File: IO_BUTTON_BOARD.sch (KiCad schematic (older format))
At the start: 135 parts, among them P1 I2C, P10 IO_7, P2 I2C, P3 IO_0, P4 IO_1, P5 IO_2, P6 IO_3, P7 IO_4, P8 IO_5, P9 IO_6, Q1 NPN, Q10 PNP, Q11 PNP, Q12 PNP, Q13 PNP, Q14 PNP, Q15 PNP, Q16 PNP, Q17 PNP, Q2 PNP, Q3 NPN, Q4 PNP, Q5 NPN, Q6 NPN, Q7 PNP, Q8 PNP, Q9 NPN, SW1 CONFIG, SW10 SW_Push, SW11 SW_Push, SW12 SW_Push, SW13 SW_Push, SW14 SW_Push, SW15 SW_Push, SW16 SW_Push, SW17 SW_Push, SW2 SW_0, SW3 SW_1, SW4 SW_2, SW5 SW_3, SW6 SW_4, SW7 SW_5, SW8 SW_6, SW9 SW_7, U1 PCF8574A, U2 74HC86, U3 74HC86

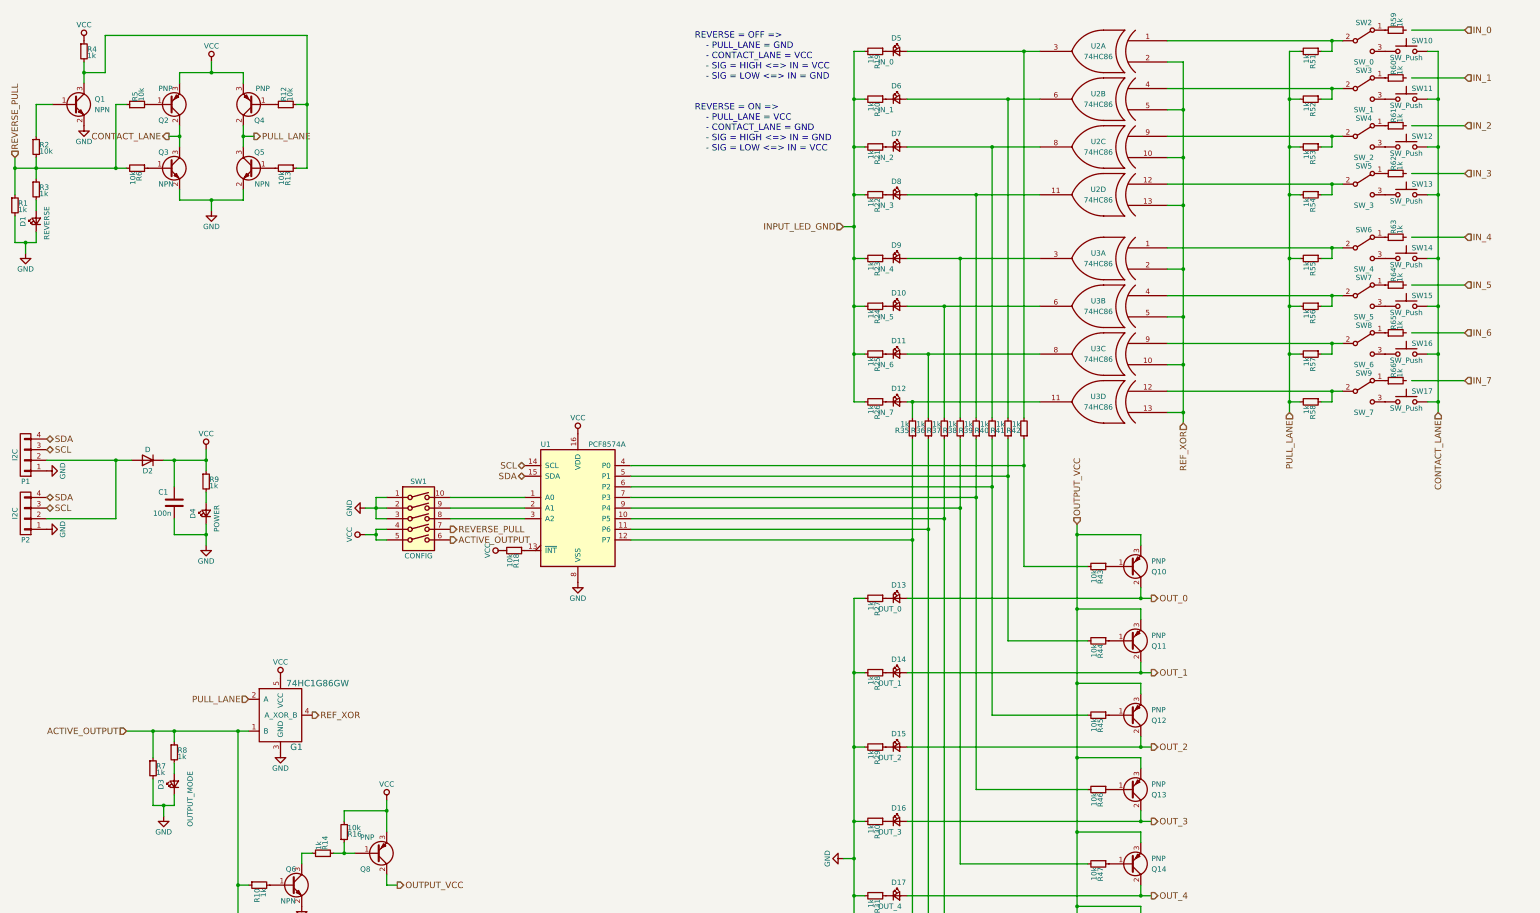
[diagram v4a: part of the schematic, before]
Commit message: Add manual routing, XOR gates remains to be routed
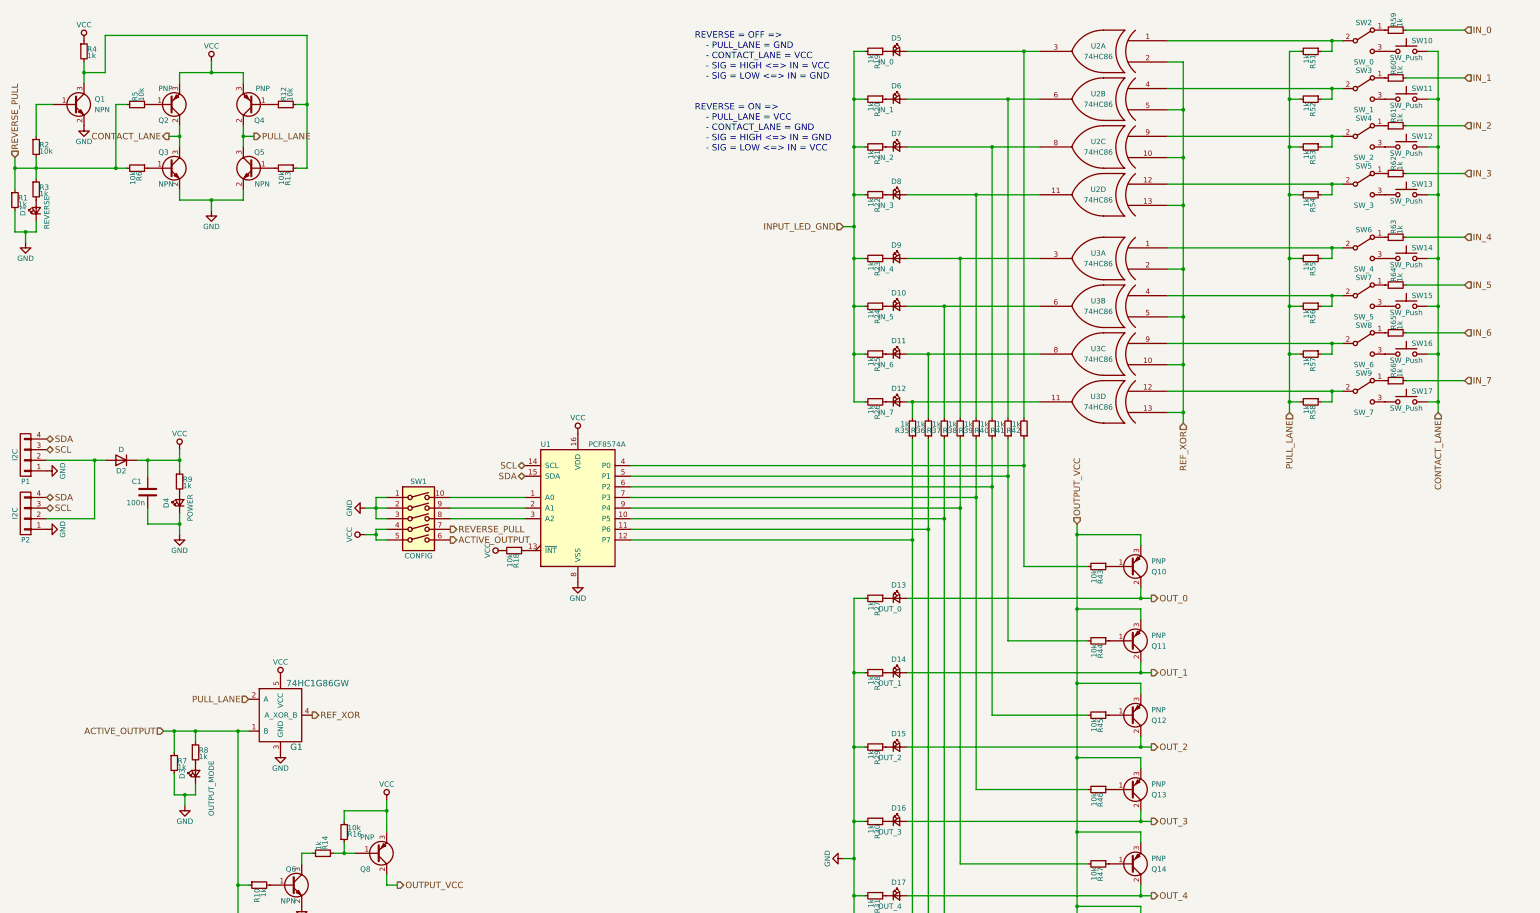
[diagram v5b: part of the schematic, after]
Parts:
- D2: footprint Diodes_SMD:DO-214AB_Handsoldering -> Diodes_SMD:DO-214AB
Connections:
- net IN_0: now also R59.2
- net IN_1: now also R60.2
- net IN_2: now also R61.2
- net IN_3: now also R62.2
- net IN_4: now also R63.2
- net IN_5: now also R64.2
- net IN_6: now also R65.2
- net IN_7: now also R66.2
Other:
- moved on the sheet: C1, D1, D2, D3, D4, R1, R7, R8, R9
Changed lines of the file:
@@
 Title "8_IO_BOARD"
 Date "2019-01-25"
-Rev "1.0"
+Rev "0.10"
 Comp "Mathias DELAHAYE"
 Comment1 "F4DEB"
@@
 L C C1
 U 1 1 5C4AF888
-P 2050 5050
-F 0 "C1" H 1900 5150 50  0000 L CNN
-F 1 "100n" H 1850 4950 50  0000 L CNN
-F 2 "Capacitors_SMD:c_elec_4x4.5" H 2088 4900 50  0001 C CNN
-F 3 "" H 2050 5050 50  0000 C CNN
-	1    2050 5050
+P 1800 4950
+F 0 "C1" H 1650 5050 50  0000 L CNN
+F 1 "100n" H 1600 4850 50  0000 L CNN
+F 2 "Capacitors_SMD:c_elec_4x4.5" H 1838 4800 50  0001 C CNN
+F 3 "" H 1800 4950 50  0000 C CNN
+	1    1800 4950
 	1    0    0    -1
 $EndComp
@@
 L LED_Small D4
 U 1 1 5C4B1934
-P 2350 5150
-F 0 "D4" H 2300 5275 50  0000 L CNN
-F 1 "POWER" H 2175 5050 50  0000 L CNN
-F 2 "LEDs:LED_0805" V 2350 5150 50  0001 C CNN
-F 3 "" V 2350 5150 50  0000 C CNN
-	1    2350 5150
+P 2100 5050
+F 0 "D4" H 2050 5175 50  0000 L CNN
+F 1 "POWER" H 1925 4950 50  0000 L CNN
+F 2 "LEDs:LED_0805" V 2100 5050 50  0001 C CNN
+F 3 "" V 2100 5050 50  0000 C CNN
+	1    2100 5050
 	0    -1   -1   0
 $EndComp
@@
 L R_Small R9
 U 1 1 5C4B193A
-P 2350 4850
-F 0 "R9" H 2380 4870 50  0000 L CNN
-F 1 "1k" H 2380 4810 50  0000 L CNN
-F 2 "Resistors_SMD:R_0805" H 2350 4850 50  0001 C CNN
-F 3 "" H 2350 4850 50  0000 C CNN
-	1    2350 4850
+P 2100 4850
+F 0 "R9" H 2130 4870 50  0000 L CNN
+F 1 "1k" H 2130 4810 50  0000 L CNN
+F 2 "Resistors_SMD:R_0805" H 2100 4850 50  0001 C CNN
+F 3 "" H 2100 4850 50  0000 C CNN
+	1    2100 4850
 	1    0    0    -1
 $EndComp
@@
 L R_Small R1
 U 1 1 5C4B8D83
-P 550 2250
-F 0 "R1" H 580 2270 50  0000 L CNN
-F 1 "1k" H 580 2210 50  0000 L CNN
-F 2 "Resistors_SMD:R_0805" H 550 2250 50  0001 C CNN
-F 3 "" H 550 2250 50  0000 C CNN
-	1    550  2250
+P 550 2200
+F 0 "R1" H 580 2220 50  0000 L CNN
+F 1 "1k" H 580 2160 50  0000 L CNN
+F 2 "Resistors_SMD:R_0805" H 550 2200 50  0001 C CNN
+F 3 "" H 550 2200 50  0000 C CNN
+	1    550  2200
 	1    0    0    -1
 $EndComp
@@
 L GND #PWR01
 U 1 1 5C4B8E84
-P 650 2700
-F 0 "#PWR01" H 650 2450 50  0001 C CNN
-F 1 "GND" H 650 2550 50  0000 C CNN
-F 2 "" H 650 2700 50  0000 C CNN
-F 3 "" H 650 2700 50  0000 C CNN
-	1    650  2700
+P 650 2600
+F 0 "#PWR01" H 650 2350 50  0001 C CNN
+F 1 "GND" H 650 2450 50  0000 C CNN
+F 2 "" H 650 2600 50  0000 C CNN
+F 3 "" H 650 2600 50  0000 C CNN
+	1    650  2600
 	1    0    0    -1
 $EndComp
@@
 L LED_Small D1
 U 1 1 5C4C4F1A
-P 750 2400
-F 0 "D1" H 700 2525 50  0000 L CNN
-F 1 "REVERSE" H 575 2300 50  0000 L CNN
-F 2 "LEDs:LED_0805" V 750 2400 50  0001 C CNN
-F 3 "" V 750 2400 50  0000 C CNN
-	1    750  2400
+P 750 2300
+F 0 "D1" H 700 2425 50  0000 L CNN
+F 1 "REVERSE" H 575 2200 50  0000 L CNN
+F 2 "LEDs:LED_0805" V 750 2300 50  0001 C CNN
+F 3 "" V 750 2300 50  0000 C CNN
+	1    750  2300
 	0    -1   -1   0
 $EndComp
@@
 L D D2
 U 1 1 5C6BAA14
-P 1800 4650
-F 0 "D2" H 1800 4750 50  0000 C CNN
-F 1 "D" H 1800 4550 50  0000 C CNN
-F 2 "Diodes_SMD:DO-214AB_Handsoldering" H 1800 4650 50  0001 C CNN
-F 3 "" H 1800 4650 50  0000 C CNN
-F 4 "688-0512" H 1800 4650 60  0001 C CNN "RS"
-	1    1800 4650
+P 1550 4650
+F 0 "D2" H 1550 4750 50  0000 C CNN
+F 1 "D" H 1550 4550 50  0000 C CNN
+F 2 "Diodes_SMD:DO-214AB" H 1550 4650 50  0001 C CNN
+F 3 "" H 1550 4650 50  0000 C CNN
+F 4 "688-0512" H 1550 4650 60  0001 C CNN "RS"
+	1    1550 4650
 	-1   0    0    1
 $EndComp
@@
 L VCC #PWR03
 U 1 1 5C767C53
-P 2350 4550
-F 0 "#PWR03" H 2350 4400 50  0001 C CNN
-F 1 "VCC" H 2350 4700 50  0000 C CNN
-F 2 "" H 2350 4550 50  0000 C CNN
-F 3 "" H 2350 4550 50  0000 C CNN
-	1    2350 4550
+P 2100 4550
+F 0 "#PWR03" H 2100 4400 50  0001 C CNN
+F 1 "VCC" H 2100 4700 50  0000 C CNN
+F 2 "" H 2100 4550 50  0000 C CNN
+F 3 "" H 2100 4550 50  0000 C CNN
+	1    2100 4550
 	1    0    0    -1
 $EndComp
@@
 L GND #PWR010
 U 1 1 5C7E9DBA
-P 2350 5450
-F 0 "#PWR010" H 2350 5200 50  0001 C CNN
-F 1 "GND" H 2350 5300 50  0000 C CNN
-F 2 "" H 2350 5450 50  0000 C CNN
-F 3 "" H 2350 5450 50  0000 C CNN
-	1    2350 5450
+P 2100 5350
+F 0 "#PWR010" H 2100 5100 50  0001 C CNN
+F 1 "GND" H 2100 5200 50  0000 C CNN
+F 2 "" H 2100 5350 50  0000 C CNN
+F 3 "" H 2100 5350 50  0000 C CNN
+	1    2100 5350
 	1    0    0    -1
 $EndComp
@@
 	0    1    1    0
 $EndComp
-Text HLabel 1600 7200 0    60   Input ~ 0
+Text HLabel 1950 7200 0    60   Input ~ 0
 ACTIVE_OUTPUT
 $Comp
@@
 Connection ~ 3950 5100
 Wire Wire Line
-	1500 5200 850  5200
-Wire Wire Line
-	850  4650 1650 4650
-Wire Wire Line
-	2350 5050 2350 4950
-Wire Wire Line
-	2350 4550 2350 4750
-Wire Wire Line
-	2350 5250 2350 5450
+	1300 5200 850  5200
+Wire Wire Line
+	850  4650 1400 4650
+Wire Wire Line
+	2100 4550 2100 4750
+Wire Wire Line
+	2100 5150 2100 5350
 Wire Wire Line
 	13850 800  13950 800
@@
 	3950 5300 4050 5300
 Wire Wire Line
-	550  1800 550  2150
+	550  1800 550  2100
 Wire Wire Line
 	2000 1600 2100 1600
@@
 	3300 650  3300 1900
 Wire Wire Line
-	750  2300 750  2200
-Wire Wire Line
-	550  2350 550  2600
-Wire Wire Line
-	550  2600 750  2600
-Wire Wire Line
-	750  2600 750  2500
-Wire Wire Line
-	650  2700 650  2600
-Connection ~ 650  2600
+	550  2300 550  2500
+Wire Wire Line
+	550  2500 750  2500
+Wire Wire Line
+	750  2500 750  2400
+Wire Wire Line
+	650  2600 650  2500
+Connection ~ 650  2500
 Wire Wire Line
 	1400 1000 1200 1000
@@
 Connection ~ 11150 6650
 Wire Wire Line
-	1500 4650 1500 5200
-Connection ~ 1500 4650
-Connection ~ 2050 4650
-Wire Wire Line
-	1950 4650 2350 4650
-Connection ~ 2350 4650
-Connection ~ 2350 5350
-Wire Wire Line
-	2050 4650 2050 4900
-Wire Wire Line
-	2050 5200 2050 5350
-Wire Wire Line
-	2050 5350 2350 5350
+	1300 4650 1300 5200
+Connection ~ 1300 4650
+Connection ~ 1800 4650
+Wire Wire Line
+	1700 4650 2100 4650
+Connection ~ 2100 4650
+Connection ~ 2100 5250
+Wire Wire Line
+	1800 4650 1800 4800
+Wire Wire Line
+	1800 5100 1800 5250
+Wire Wire Line
+	1800 5250 2100 5250
 Wire Wire Line
 	8950 5950 11250 5950
@@
 L R_Small R7
 U 1 1 5C821A26
-P 1850 7550
-F 0 "R7" H 1880 7570 50  0000 L CNN
-F 1 "1k" H 1880 7510 50  0000 L CNN
-F 2 "Resistors_SMD:R_0805" H 1850 7550 50  0001 C CNN
-F 3 "" H 1850 7550 50  0000 C CNN
-	1    1850 7550
+P 2050 7500
+F 0 "R7" H 2080 7520 50  0000 L CNN
+F 1 "1k" H 2080 7460 50  0000 L CNN
+F 2 "Resistors_SMD:R_0805" H 2050 7500 50  0001 C CNN
+F 3 "" H 2050 7500 50  0000 C CNN
+	1    2050 7500
 	1    0    0    -1
 $EndComp
@@
 L GND #PWR034
 U 1 1 5C821A2C
-P 1950 8000
-F 0 "#PWR034" H 1950 7750 50  0001 C CNN
-F 1 "GND" H 1950 7850 50  0000 C CNN
-F 2 "" H 1950 8000 50  0000 C CNN
-F 3 "" H 1950 8000 50  0000 C CNN
-	1    1950 8000
+P 2150 7900
+F 0 "#PWR034" H 2150 7650 50  0001 C CNN
+F 1 "GND" H 2150 7750 50  0000 C CNN
+F 2 "" H 2150 7900 50  0000 C CNN
+F 3 "" H 2150 7900 50  0000 C CNN
+	1    2150 7900
 	1    0    0    -1
 $EndComp
@@
 L R_Small R8
 U 1 1 5C821A32
-P 2050 7400
-F 0 "R8" H 2080 7420 50  0000 L CNN
-F 1 "1k" H 2080 7360 50  0000 L CNN
-F 2 "Resistors_SMD:R_0805" H 2050 7400 50  0001 C CNN
-F 3 "" H 2050 7400 50  0000 C CNN
-	1    2050 7400
+P 2250 7400
+F 0 "R8" H 2280 7420 50  0000 L CNN
+F 1 "1k" H 2280 7360 50  0000 L CNN
+F 2 "Resistors_SMD:R_0805" H 2250 7400 50  0001 C CNN
+F 3 "" H 2250 7400 50  0000 C CNN
+	1    2250 7400
 	1    0    0    -1
 $EndComp
@@
 L LED_Small D3
 U 1 1 5C821A38
-P 2050 7700
-F 0 "D3" H 2000 7825 50  0000 L CNN
-F 1 "OUTPUT_MODE" H 1650 7550 50  0000 L CNN
-F 2 "LEDs:LED_0805" V 2050 7700 50  0001 C CNN
-F 3 "" V 2050 7700 50  0000 C CNN
-	1    2050 7700
+P 2250 7600
+F 0 "D3" H 2200 7725 50  0000 L CNN
+F 1 "OUTPUT_MODE" H 1850 7450 50  0000 L CNN
+F 2 "LEDs:LED_0805" V 2250 7600 50  0001 C CNN
+F 3 "" V 2250 7600 50  0000 C CNN
+	1    2250 7600
 	0    -1   -1   0
 $EndComp
 Wire Wire Line
-	1850 7200 1850 7450
-Wire Wire Line
-	2050 7600 2050 7500
-Wire Wire Line
-	1850 7650 1850 7900
-Wire Wire Line
-	1850 7900 2050 7900
-Wire Wire Line
-	2050 7900 2050 7800
-Wire Wire Line
-	1950 8000 1950 7900
-Connection ~ 1950 7900
-Wire Wire Line
-	2050 7200 2050 7300
+	2050 7200 2050 7400
+Wire Wire Line
+	2050 7600 2050 7800
+Wire Wire Line
+	2050 7800 2250 7800
+Wire Wire Line
+	2250 7800 2250 7700
+Wire Wire Line
+	2150 7900 2150 7800
+Connection ~ 2150 7800
+Wire Wire Line
+	2250 7200 2250 7300
+Connection ~ 2250 7200
 Connection ~ 2050 7200
-Connection ~ 1850 7200
 $Comp
 L 74HC1G86GW G1
@@
 REF_XOR
 Wire Wire Line
-	1600 7200 2750 7200
+	1950 7200 2750 7200
 Wire Wire Line
 	2650 7200 2650 10100
@@
 $EndComp
 Wire Wire Line
-	13700 3000 14200 3000
+	13650 3000 14200 3000
 $Comp
 L R_Small R65
@@
 $EndComp
 Wire Wire Line
-	13700 3900 14200 3900
-Wire Wire Line
-	14200 3450 13700 3450
-Wire Wire Line
-	13700 2550 14200 2550
-Wire Wire Line
-	13700 1950 14200 1950
-Wire Wire Line
-	13700 1500 14200 1500
-Wire Wire Line
-	14200 1050 13700 1050
-Wire Wire Line
-	13700 600  14200 600
+	13650 3900 14200 3900
+Wire Wire Line
+	14200 3450 13650 3450
+Wire Wire Line
+	13650 2550 14200 2550
+Wire Wire Line
+	13650 1950 14200 1950
+Wire Wire Line
+	13650 1500 14200 1500
+Wire Wire Line
+	14200 1050 13650 1050
+Wire Wire Line
+	13650 600  14200 600
 $EndSCHEMATC
